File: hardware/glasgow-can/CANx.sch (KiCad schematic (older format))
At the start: 13 parts, among them Q1 TLP240A, U1 TCAN1051

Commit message: minor tweaks
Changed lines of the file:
@@
 $Descr A4 11693 8268
 encoding utf-8
-Sheet 2 3
+Sheet 3 3
 Title "Glasgow CAN Add-On"
-Date "2020-11-20"
+Date "2020-12-19"
 Rev "r0"
 Comp ""
@@
 AR Path="/5FCD3D33/5FBD7E1E" Ref="U?"  Part="1"
 AR Path="/5FD1E469/5FBD7E1E" Ref="U2"  Part="1"
-F 0 "U1" H 4400 3600 50  0000 L CNN
+F 0 "U2" H 4400 3600 50  0000 L CNN
 F 1 "TCAN1051" H 4650 3624 50  0001 C CNN
 F 2 "Package_DFN_QFN:DFN-8-1EP_3x3mm_P0.65mm_EP1.7x2.05mm" H 4400 2550 50  0001 L CNN
@@
 AR Path="/5FCD3D33/5FBD84AB" Ref="#PWR?"  Part="1"
 AR Path="/5FD1E469/5FBD84AB" Ref="#PWR014"  Part="1"
-F 0 "#PWR09" H 4150 3450 50  0001 C CNN
+F 0 "#PWR014" H 4150 3450 50  0001 C CNN
 F 1 "0V" H 4155 3477 50  0000 C CNN
 F 2 "" H 3850 3750 50  0001 C CNN
@@
 AR Path="/5FCD3D33/5FBE90CB" Ref="Q?"  Part="1"
 AR Path="/5FD1E469/5FBE90CB" Ref="Q3"  Part="1"
-F 0 "Q1" H 7050 3600 50  0000 L CNN
+F 0 "Q3" H 7050 3600 50  0000 L CNN
 F 1 "TLP240A" H 7300 2750 50  0000 C CNN
 F 2 "glasgow-can:TLP240A_5" H 7050 2650 50  0001 L CNN
@@
 AR Path="/5FCD3D33/5FBEAE62" Ref="#PWR?"  Part="1"
 AR Path="/5FD1E469/5FBEAE62" Ref="#PWR013"  Part="1"
-F 0 "#PWR08" H 6850 3350 50  0001 C CNN
+F 0 "#PWR013" H 6850 3350 50  0001 C CNN
 F 1 "0V" H 6855 3377 50  0000 C CNN
 F 2 "" H 6550 3650 50  0001 C CNN
@@
 AR Path="/5FCD3D33/5FBEBE4B" Ref="R?"  Part="1"
 AR Path="/5FD1E469/5FBEBE4B" Ref="R7"  Part="1"
-F 0 "R1" V 7900 2650 50  0000 C TNN
+F 0 "R7" V 7900 2650 50  0000 C TNN
 F 1 "120" V 7800 2650 50  0000 C BNN
 F 2 "Resistor_SMD:R_1206_3216Metric" H 7850 2650 50  0001 C CNN
@@
 AR Path="/5FCD3D33/5FBEA8CB" Ref="R?"  Part="1"
 AR Path="/5FD1E469/5FBEA8CB" Ref="R8"  Part="1"
-F 0 "R2" V 6650 2950 50  0000 C BNN
+F 0 "R8" V 6650 2950 50  0000 C BNN
 F 1 "510" V 6750 2950 50  0000 C TNN
 F 2 "Resistor_SMD:R_0402_1005Metric" H 6700 2950 50  0001 C CNN
@@
 AR Path="/5FCD3D33/5FBF5E92" Ref="D?"  Part="1"
 AR Path="/5FD1E469/5FBF5E92" Ref="D5"  Part="1"
-F 0 "D1" H 8600 3350 50  0000 C CNN
+F 0 "D5" H 8600 3350 50  0000 C CNN
 F 1 "PESD2CAN" H 8600 3250 50  0000 C CNN
 F 2 "rhais_package-smd:SOT-23" H 8450 3100 50  0001 C CNN
@@
 AR Path="/5FCD3D33/5FBF694A" Ref="#PWR?"  Part="1"
 AR Path="/5FD1E469/5FBF694A" Ref="#PWR012"  Part="1"
-F 0 "#PWR07" H 8850 2900 50  0001 C CNN
+F 0 "#PWR012" H 8850 2900 50  0001 C CNN
 F 1 "0V" V 8855 2972 50  0000 R CNN
 F 2 "" H 8550 3200 50  0001 C CNN
@@
 AR Path="/5FCD3D33/5FC20CDB" Ref="#PWR?"  Part="1"
 AR Path="/5FD1E469/5FC20CDB" Ref="#PWR011"  Part="1"
-F 0 "#PWR06" H 4450 1850 50  0001 C CNN
+F 0 "#PWR011" H 4450 1850 50  0001 C CNN
 F 1 "0V" H 4455 1877 50  0000 C CNN
 F 2 "" H 4150 2150 50  0001 C CNN
@@
 AR Path="/5FCD3D33/5FC25A3E" Ref="C?"  Part="1"
 AR Path="/5FD1E469/5FC25A3E" Ref="C4"  Part="1"
-F 0 "C2" V 4750 1750 50  0000 C BNN
+F 0 "C4" V 4750 1750 50  0000 C BNN
 F 1 "4.7u" V 4950 1750 50  0000 C TNN
 F 2 "Capacitor_SMD:C_0603_1608Metric" H 4850 1750 50  0001 C CNN
@@
 AR Path="/5FCD3D33/5FC25EC7" Ref="C?"  Part="1"
 AR Path="/5FD1E469/5FC25EC7" Ref="C3"  Part="1"
-F 0 "C1" V 4350 1750 50  0000 C BNN
+F 0 "C3" V 4350 1750 50  0000 C BNN
 F 1 "100n" V 4550 1750 50  0000 C TNN
 F 2 "Capacitor_SMD:C_0402_1005Metric" H 4450 1750 50  0001 C CNN
@@
 AR Path="/5FCD3D33/5FC08BB3" Ref="#PWR?"  Part="1"
 AR Path="/5FD1E469/5FC08BB3" Ref="#PWR015"  Part="1"
-F 0 "#PWR010" H 2700 6200 50  0001 C CNN
+F 0 "#PWR015" H 2700 6200 50  0001 C CNN
 F 1 "0V" H 2705 6227 50  0000 C CNN
 F 2 "" H 2400 6500 50  0001 C CNN
@@
 AR Path="/5FCD3D33/5FC897F6" Ref="D?"  Part="1"
 AR Path="/5FD1E469/5FC897F6" Ref="D6"  Part="1"
-F 0 "D2" H 2700 5600 50  0000 C BNN
+F 0 "D6" H 2700 5600 50  0000 C BNN
 F 1 "TJ-S1005SW4TGLC0A-A5" H 2700 5400 50  0000 C CNN
 F 2 "LED_SMD:LED_0402_1005Metric_Pad0.77x0.64mm_HandSolder" V 2700 5500 50  0001 C CNN
@@
 AR Path="/5FCD3D33/5FC8FDFC" Ref="R?"  Part="1"
 AR Path="/5FD1E469/5FC8FDFC" Ref="R11"  Part="1"
-F 0 "R5" V 3550 6150 50  0000 C BNN
+F 0 "R11" V 3550 6150 50  0000 C BNN
 F 1 "25k" V 3650 6150 50  0000 C TNN
 F 2 "Resistor_SMD:R_0402_1005Metric" H 3600 6150 50  0001 C CNN
@@
 AR Path="/5FCD3D33/5FC8FE04" Ref="R?"  Part="1"
 AR Path="/5FD1E469/5FC8FE04" Ref="R10"  Part="1"
-F 0 "R4" V 3100 6150 50  0000 C BNN
+F 0 "R10" V 3100 6150 50  0000 C BNN
 F 1 "100k" V 3200 6150 50  0000 C TNN
 F 2 "Resistor_SMD:R_0402_1005Metric" H 3150 6150 50  0001 C CNN
@@
 AR Path="/5FCD3D33/5FC94AD6" Ref="R?"  Part="1"
 AR Path="/5FD1E469/5FC94AD6" Ref="R9"  Part="1"
-F 0 "R3" V 2650 6150 50  0000 C BNN
+F 0 "R9" V 2650 6150 50  0000 C BNN
 F 1 "25k" V 2750 6150 50  0000 C TNN
 F 2 "Resistor_SMD:R_0402_1005Metric" H 2700 6150 50  0001 C CNN
@@
 AR Path="/5FCD3D33/5FCB8AEE" Ref="D?"  Part="1"
 AR Path="/5FD1E469/5FCB8AEE" Ref="D7"  Part="1"
-F 0 "D3" H 3150 5600 50  0000 C BNN
+F 0 "D7" H 3150 5600 50  0000 C BNN
 F 1 "TJ-S1005SW4TGLC2G-A5" H 3150 5400 50  0000 C CNN
 F 2 "LED_SMD:LED_0402_1005Metric_Pad0.77x0.64mm_HandSolder" V 3150 5500 50  0001 C CNN
@@
 AR Path="/5FCD3D33/5FCB8E6D" Ref="D?"  Part="1"
 AR Path="/5FD1E469/5FCB8E6D" Ref="D8"  Part="1"
-F 0 "D4" H 3600 5600 50  0000 C BNN
+F 0 "D8" H 3600 5600 50  0000 C BNN
 F 1 "TJ-S1005SW4TGLC0A-A5" H 3600 5400 50  0000 C CNN
 F 2 "LED_SMD:LED_0402_1005Metric_Pad0.77x0.64mm_HandSolder" V 3600 5500 50  0001 C CNN

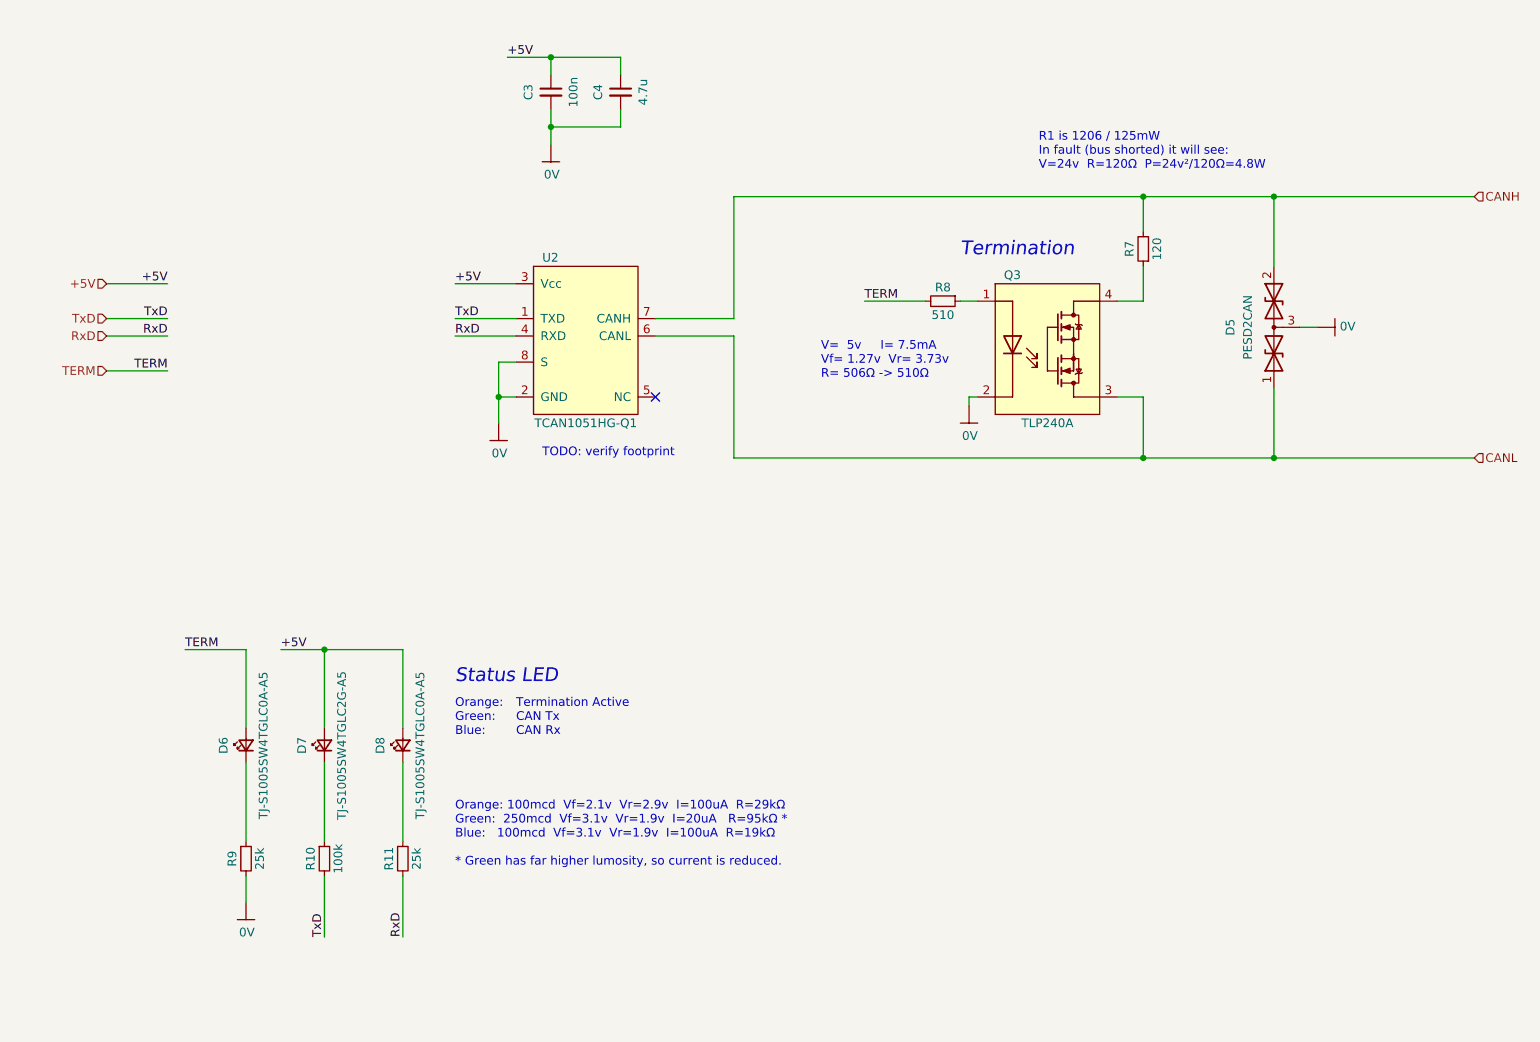
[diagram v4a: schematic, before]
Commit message: tweak LEDs for availability, and revise CAN line driver part number
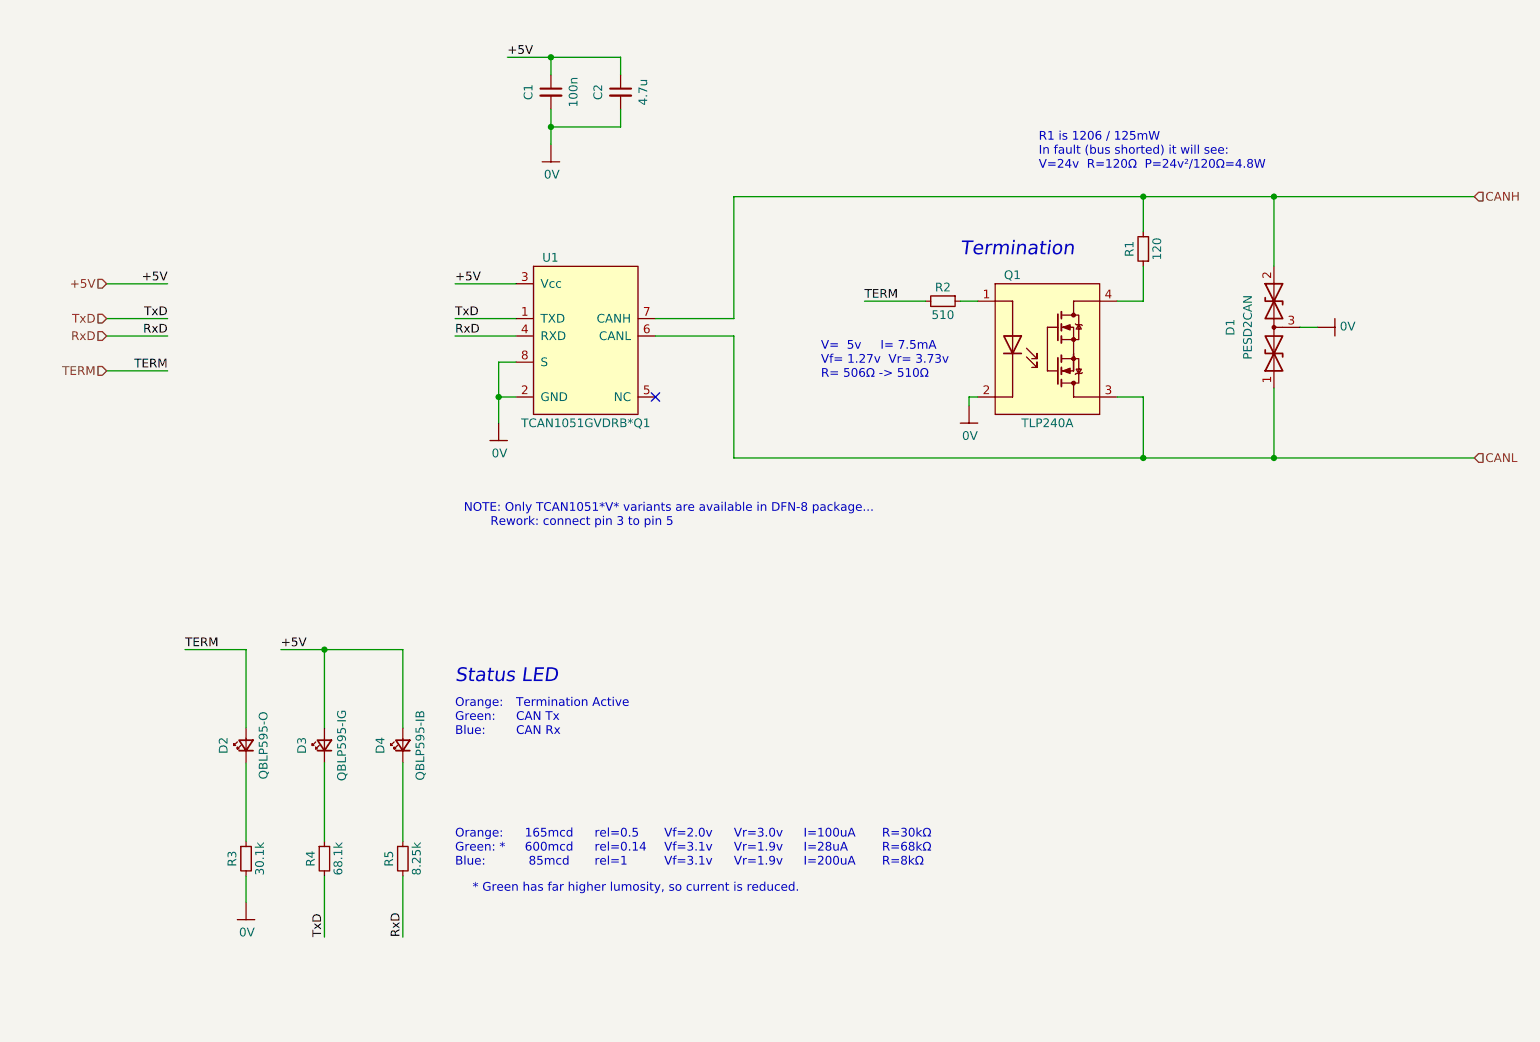
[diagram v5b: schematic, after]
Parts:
- D2: value TJ-S1005SW4TGLC0A-A5 -> QBLP595-O; MFR TOGIALED -> QT Brightek; MPN TJ-S1005SW4TGLC0A-A5 -> QBLP595-O
- D3: value TJ-S1005SW4TGLC2G-A5 -> QBLP595-IG; MFR TOGIALED -> QT Brightek; MPN TJ-S1005SW4TGLC2G-A5 -> QBLP595-IG
- D4: value TJ-S1005SW4TGLC0A-A5 -> QBLP595-IB; MFR TOGIALED -> QT Brightek; MPN TJ-S1005SW4TGLC0A-A5 -> QBLP595-IB
- R3: value 25k -> 30.1k
- R4: value 100k -> 68.1k
- R5: value 25k -> 8.25k
- U1: MPN TCAN1051HG-Q1 -> TCAN1051GVDRB*Q1
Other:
- note added: "* Green has far higher lumosity, so current is reduced."
- note added: "165mcd\n600mcd\n 85mcd"
- note added: "I=100uA\nI=28uA\nI=200uA"
- note added: "NOTE: Only TCAN1051*V* variants are available in DFN-8 package...\n Rework: connect pin 3 to pin 5\n"
- note added: "Orange:\nGreen: *\nBlue:"
- note added: "R=30kΩ\nR=68kΩ\nR=8kΩ"
- note added: "Vf=2.0v\nVf=3.1v\nVf=3.1v"
- note added: "Vr=3.0v\nVr=1.9v\nVr=1.9v"
- note added: "rel=0.5\nrel=0.14\nrel=1"
- note removed: "Orange: 100mcd Vf=2.1v Vr=2.9v I=100uA R=29kΩ\nGreen: 250mcd Vf=3.1v Vr=1.9v I=20uA R=95kΩ *\nBlue: 100mcd Vf=3.1v Vr=1.9v I=100uA R=19kΩ\n\n* Green has far higher lumosity, so current is reduced."
- note removed: "TODO: verify footprint"
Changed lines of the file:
@@
 $Descr A4 11693 8268
 encoding utf-8
-Sheet 3 3
+Sheet 2 3
 Title "Glasgow CAN Add-On"
 Date "2020-12-19"
@@
 AR Path="/5FCD3D33/5FBD7E1E" Ref="U?"  Part="1"
 AR Path="/5FD1E469/5FBD7E1E" Ref="U2"  Part="1"
-F 0 "U2" H 4400 3600 50  0000 L CNN
+F 0 "U1" H 4400 3600 50  0000 L CNN
 F 1 "TCAN1051" H 4650 3624 50  0001 C CNN
 F 2 "Package_DFN_QFN:DFN-8-1EP_3x3mm_P0.65mm_EP1.7x2.05mm" H 4400 2550 50  0001 L CNN
 F 3 "" H 4650 3150 50  0001 C CNN
-F 4 "TCAN1051HG-Q1" H 4650 2650 50  0000 C CNN "MPN"
+F 4 "TCAN1051GVDRB*Q1" H 4650 2650 50  0000 C CNN "MPN"
 F 5 "Texas Instruments" H 4650 3150 50  0001 C CNN "MFR"
 	1    4650 3150
@@
 AR Path="/5FCD3D33/5FBD84AB" Ref="#PWR?"  Part="1"
 AR Path="/5FD1E469/5FBD84AB" Ref="#PWR014"  Part="1"
-F 0 "#PWR014" H 4150 3450 50  0001 C CNN
+F 0 "#PWR09" H 4150 3450 50  0001 C CNN
 F 1 "0V" H 4155 3477 50  0000 C CNN
 F 2 "" H 3850 3750 50  0001 C CNN
@@
 AR Path="/5FCD3D33/5FBE90CB" Ref="Q?"  Part="1"
 AR Path="/5FD1E469/5FBE90CB" Ref="Q3"  Part="1"
-F 0 "Q3" H 7050 3600 50  0000 L CNN
+F 0 "Q1" H 7050 3600 50  0000 L CNN
 F 1 "TLP240A" H 7300 2750 50  0000 C CNN
 F 2 "glasgow-can:TLP240A_5" H 7050 2650 50  0001 L CNN
@@
 AR Path="/5FCD3D33/5FBEAE62" Ref="#PWR?"  Part="1"
 AR Path="/5FD1E469/5FBEAE62" Ref="#PWR013"  Part="1"
-F 0 "#PWR013" H 6850 3350 50  0001 C CNN
+F 0 "#PWR08" H 6850 3350 50  0001 C CNN
 F 1 "0V" H 6855 3377 50  0000 C CNN
 F 2 "" H 6550 3650 50  0001 C CNN
@@
 AR Path="/5FCD3D33/5FBEBE4B" Ref="R?"  Part="1"
 AR Path="/5FD1E469/5FBEBE4B" Ref="R7"  Part="1"
-F 0 "R7" V 7900 2650 50  0000 C TNN
+F 0 "R1" V 7900 2650 50  0000 C TNN
 F 1 "120" V 7800 2650 50  0000 C BNN
 F 2 "Resistor_SMD:R_1206_3216Metric" H 7850 2650 50  0001 C CNN
@@
 AR Path="/5FCD3D33/5FBEA8CB" Ref="R?"  Part="1"
 AR Path="/5FD1E469/5FBEA8CB" Ref="R8"  Part="1"
-F 0 "R8" V 6650 2950 50  0000 C BNN
+F 0 "R2" V 6650 2950 50  0000 C BNN
 F 1 "510" V 6750 2950 50  0000 C TNN
 F 2 "Resistor_SMD:R_0402_1005Metric" H 6700 2950 50  0001 C CNN
@@
 AR Path="/5FCD3D33/5FBF5E92" Ref="D?"  Part="1"
 AR Path="/5FD1E469/5FBF5E92" Ref="D5"  Part="1"
-F 0 "D5" H 8600 3350 50  0000 C CNN
+F 0 "D1" H 8600 3350 50  0000 C CNN
 F 1 "PESD2CAN" H 8600 3250 50  0000 C CNN
 F 2 "rhais_package-smd:SOT-23" H 8450 3100 50  0001 C CNN
@@
 AR Path="/5FCD3D33/5FBF694A" Ref="#PWR?"  Part="1"
 AR Path="/5FD1E469/5FBF694A" Ref="#PWR012"  Part="1"
-F 0 "#PWR012" H 8850 2900 50  0001 C CNN
+F 0 "#PWR07" H 8850 2900 50  0001 C CNN
 F 1 "0V" V 8855 2972 50  0000 R CNN
 F 2 "" H 8550 3200 50  0001 C CNN
@@
 	4250 3050 3900 3050
 Text Notes 3900 6200 0    50   ~ 0
-Orange: 100mcd  Vf=2.1v  Vr=2.9v  I=100uA  R=29kΩ\nGreen:  250mcd  Vf=3.1v  Vr=1.9v  I=20uA   R=95kΩ *\nBlue:   100mcd  Vf=3.1v  Vr=1.9v  I=100uA  R=19kΩ\n\n* Green has far higher lumosity, so current is reduced.
+Orange:\nGreen: *\nBlue:
 Text Label 4200 1550 0    50   ~ 0
 +5V
@@
 AR Path="/5FCD3D33/5FC20CDB" Ref="#PWR?"  Part="1"
 AR Path="/5FD1E469/5FC20CDB" Ref="#PWR011"  Part="1"
-F 0 "#PWR011" H 4450 1850 50  0001 C CNN
+F 0 "#PWR06" H 4450 1850 50  0001 C CNN
 F 1 "0V" H 4455 1877 50  0000 C CNN
 F 2 "" H 4150 2150 50  0001 C CNN
@@
 AR Path="/5FCD3D33/5FC25A3E" Ref="C?"  Part="1"
 AR Path="/5FD1E469/5FC25A3E" Ref="C4"  Part="1"
-F 0 "C4" V 4750 1750 50  0000 C BNN
+F 0 "C2" V 4750 1750 50  0000 C BNN
 F 1 "4.7u" V 4950 1750 50  0000 C TNN
 F 2 "Capacitor_SMD:C_0603_1608Metric" H 4850 1750 50  0001 C CNN
@@
 AR Path="/5FCD3D33/5FC25EC7" Ref="C?"  Part="1"
 AR Path="/5FD1E469/5FC25EC7" Ref="C3"  Part="1"
-F 0 "C3" V 4350 1750 50  0000 C BNN
+F 0 "C1" V 4350 1750 50  0000 C BNN
 F 1 "100n" V 4550 1750 50  0000 C TNN
 F 2 "Capacitor_SMD:C_0402_1005Metric" H 4450 1750 50  0001 C CNN
@@
 Text Notes 7250 2200 0    50   ~ 0
 R1 is 1206 / 125mW\nIn fault (bus shorted) it will see:\nV=24v  R=120Ω  P=24v²/120Ω=4.8W
-Text Notes 4400 3850 0    50   ~ 0
-TODO: verify footprint
 Wire Wire Line
 	4200 1550 4450 1550
@@
 AR Path="/5FCD3D33/5FC08BB3" Ref="#PWR?"  Part="1"
 AR Path="/5FD1E469/5FC08BB3" Ref="#PWR015"  Part="1"
-F 0 "#PWR015" H 2700 6200 50  0001 C CNN
+F 0 "#PWR010" H 2700 6200 50  0001 C CNN
 F 1 "0V" H 2705 6227 50  0000 C CNN
 F 2 "" H 2400 6500 50  0001 C CNN
@@
 Text Label 2350 4950 0    50   ~ 0
 TERM
-$Comp
-L Device:LED_Small D2
-U 1 1 5FC897F6
-P 2700 5500
-AR Path="/5FB9C48E/5FC897F6" Ref="D2"  Part="1"
-AR Path="/5FBB2899/5FC897F6" Ref="D?"  Part="1"
-AR Path="/5FCD3D33/5FC897F6" Ref="D?"  Part="1"
-AR Path="/5FD1E469/5FC897F6" Ref="D6"  Part="1"
-F 0 "D6" H 2700 5600 50  0000 C BNN
-F 1 "TJ-S1005SW4TGLC0A-A5" H 2700 5400 50  0000 C CNN
-F 2 "LED_SMD:LED_0402_1005Metric_Pad0.77x0.64mm_HandSolder" V 2700 5500 50  0001 C CNN
-F 3 "~" V 2700 5500 50  0001 C CNN
-F 4 "TOGIALED" H 2700 5500 50  0001 C CNN "MFR"
-F 5 "TJ-S1005SW4TGLC0A-A5" H 2700 5500 50  0001 C CNN "MPN"
-	1    2700 5500
-	0    -1   -1   0
-$EndComp
 Text Label 2900 4950 0    50   ~ 0
 +5V
@@
 AR Path="/5FCD3D33/5FC8FDFC" Ref="R?"  Part="1"
 AR Path="/5FD1E469/5FC8FDFC" Ref="R11"  Part="1"
-F 0 "R11" V 3550 6150 50  0000 C BNN
-F 1 "25k" V 3650 6150 50  0000 C TNN
+F 0 "R5" V 3550 6150 50  0000 C BNN
+F 1 "8.25k" V 3650 6150 50  0000 C TNN
 F 2 "Resistor_SMD:R_0402_1005Metric" H 3600 6150 50  0001 C CNN
 F 3 "~" H 3600 6150 50  0001 C CNN
@@
 AR Path="/5FCD3D33/5FC8FE04" Ref="R?"  Part="1"
 AR Path="/5FD1E469/5FC8FE04" Ref="R10"  Part="1"
-F 0 "R10" V 3100 6150 50  0000 C BNN
-F 1 "100k" V 3200 6150 50  0000 C TNN
+F 0 "R4" V 3100 6150 50  0000 C BNN
+F 1 "68.1k" V 3200 6150 50  0000 C TNN
 F 2 "Resistor_SMD:R_0402_1005Metric" H 3150 6150 50  0001 C CNN
 F 3 "~" H 3150 6150 50  0001 C CNN
@@
 AR Path="/5FCD3D33/5FC94AD6" Ref="R?"  Part="1"
 AR Path="/5FD1E469/5FC94AD6" Ref="R9"  Part="1"
-F 0 "R9" V 2650 6150 50  0000 C BNN
-F 1 "25k" V 2750 6150 50  0000 C TNN
+F 0 "R3" V 2650 6150 50  0000 C BNN
+F 1 "30.1k" V 2750 6150 50  0000 C TNN
 F 2 "Resistor_SMD:R_0402_1005Metric" H 2700 6150 50  0001 C CNN
 F 3 "~" H 2700 6150 50  0001 C CNN
@@
 Text Notes 4250 5450 0    50   ~ 0
 Termination Active\nCAN Tx\nCAN Rx
+Wire Wire Line
+	3150 4950 3600 4950
+Connection ~ 3150 4950
+Wire Wire Line
+	2900 4950 3150 4950
+Wire Wire Line
+	4150 3500 4150 3300
+Wire Wire Line
+	4150 3300 4250 3300
+Connection ~ 4150 3500
+Text Notes 3950 4250 0    50   ~ 0
+NOTE: Only TCAN1051*V* variants are available in DFN-8 package...\n       Rework: connect pin 3 to pin 5\n
+$Comp
+L Device:LED_Small D2
+U 1 1 5FC897F6
+P 2700 5500
+AR Path="/5FB9C48E/5FC897F6" Ref="D2"  Part="1"
+AR Path="/5FBB2899/5FC897F6" Ref="D?"  Part="1"
+AR Path="/5FCD3D33/5FC897F6" Ref="D?"  Part="1"
+AR Path="/5FD1E469/5FC897F6" Ref="D6"  Part="1"
+F 0 "D2" H 2700 5600 50  0000 C BNN
+F 1 "QBLP595-O" H 2700 5400 50  0000 C CNN
+F 2 "LED_SMD:LED_0402_1005Metric_Pad0.77x0.64mm_HandSolder" V 2700 5500 50  0001 C CNN
+F 3 "~" V 2700 5500 50  0001 C CNN
+F 4 "QT Brightek" H 2700 5500 50  0001 C CNN "MFR"
+F 5 "QBLP595-O" H 2700 5500 50  0001 C CNN "MPN"
+	1    2700 5500
+	0    -1   -1   0
+$EndComp
 $Comp
 L Device:LED_Small D3
@@
 AR Path="/5FCD3D33/5FCB8AEE" Ref="D?"  Part="1"
 AR Path="/5FD1E469/5FCB8AEE" Ref="D7"  Part="1"
-F 0 "D7" H 3150 5600 50  0000 C BNN
-F 1 "TJ-S1005SW4TGLC2G-A5" H 3150 5400 50  0000 C CNN
+F 0 "D3" H 3150 5600 50  0000 C BNN
+F 1 "QBLP595-IG" H 3150 5400 50  0000 C CNN
 F 2 "LED_SMD:LED_0402_1005Metric_Pad0.77x0.64mm_HandSolder" V 3150 5500 50  0001 C CNN
 F 3 "~" V 3150 5500 50  0001 C CNN
-F 4 "TOGIALED" H 3150 5500 50  0001 C CNN "MFR"
-F 5 "TJ-S1005SW4TGLC2G-A5" H 3150 5500 50  0001 C CNN "MPN"
+F 4 "QT Brightek" H 3150 5500 50  0001 C CNN "MFR"
+F 5 "QBLP595-IG" H 3150 5500 50  0001 C CNN "MPN"
 	1    3150 5500
 	0    -1   -1   0
@@
 AR Path="/5FCD3D33/5FCB8E6D" Ref="D?"  Part="1"
 AR Path="/5FD1E469/5FCB8E6D" Ref="D8"  Part="1"
-F 0 "D8" H 3600 5600 50  0000 C BNN
-F 1 "TJ-S1005SW4TGLC0A-A5" H 3600 5400 50  0000 C CNN
+F 0 "D4" H 3600 5600 50  0000 C BNN
+F 1 "QBLP595-IB" H 3600 5400 50  0000 C CNN
 F 2 "LED_SMD:LED_0402_1005Metric_Pad0.77x0.64mm_HandSolder" V 3600 5500 50  0001 C CNN
 F 3 "~" V 3600 5500 50  0001 C CNN
-F 4 "TOGIALED" H 3600 5500 50  0001 C CNN "MFR"
-F 5 "TJ-S1005SW4TGLC0A-A5" H 3600 5500 50  0001 C CNN "MPN"
+F 4 "QT Brightek" H 3600 5500 50  0001 C CNN "MFR"
+F 5 "QBLP595-IB" H 3600 5500 50  0001 C CNN "MPN"
 	1    3600 5500
 	0    -1   -1   0
 $EndComp
-Wire Wire Line
-	3150 4950 3600 4950
-Connection ~ 3150 4950
-Wire Wire Line
-	2900 4950 3150 4950
-Wire Wire Line
-	4150 3500 4150 3300
-Wire Wire Line
-	4150 3300 4250 3300
-Connection ~ 4150 3500
+Text Notes 4300 6200 0    50   ~ 0
+165mcd\n600mcd\n 85mcd
+Text Notes 4700 6200 0    50   ~ 0
+rel=0.5\nrel=0.14\nrel=1
+Text Notes 5100 6200 0    50   ~ 0
+Vf=2.0v\nVf=3.1v\nVf=3.1v
+Text Notes 5500 6200 0    50   ~ 0
+Vr=3.0v\nVr=1.9v\nVr=1.9v
+Text Notes 5900 6200 0    50   ~ 0
+I=100uA\nI=28uA\nI=200uA
+Text Notes 6350 6200 0    50   ~ 0
+R=30kΩ\nR=68kΩ\nR=8kΩ
+Text Notes 4000 6350 0    50   ~ 0
+* Green has far higher lumosity, so current is reduced.
 $EndSCHEMATC
